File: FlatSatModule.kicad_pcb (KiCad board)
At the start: 2 copper layers, 204.5 x 269.5 mm, 2 parts, among them J101 DB26_Male_HighDensity_Mountin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

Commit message: first routing, lost schematic
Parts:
- added D1: LED, LED_SMD:LED_0805_2012Metric_Pad1.15x1.40mm_HandSolder, F.Cu at (91.4, 139.7)
- added D2: LED, LED_SMD:LED_0805_2012Metric_Pad1.15x1.40mm_HandSolder, F.Cu at (64.8, 53.3)
- added J1: HEADER_13x2, Connector_PinHeader_2.54mm:PinHeader_2x13_P2.54mm_Vertical, F.Cu at (76.2, 69.8)
- added J2: Micro_SD_Card_Det, Connector_Card:microSD_HC_Hirose_DM3D-SF, F.Cu at (91.4, 152.4)
- moved J101 126.6 mm to (83.8, 49.5), turned to 180 degrees
- moved stm32101 57.9 mm to (93.4, 99.9)
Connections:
- J101 pad 1: (no net) -> /SPI4_MOSI
- J101 pad 10: (no net) -> /SPI4_SS
- J101 pad 11: (no net) -> /SPI4_SCK
- J101 pad 12: (no net) -> /I2C1_SCL
- J101 pad 13: (no net) -> /I2C3_SDA
- J101 pad 14: (no net) -> Net-(J101-Pad14)
- J101 pad 15: (no net) -> Net-(J101-Pad15)
- J101 pad 16: (no net) -> Net-(J101-Pad16)
- J101 pad 17: (no net) -> Net-(J101-Pad17)
- J101 pad 18: (no net) -> GND
- J101 pad 19: (no net) -> /SPI4_MISO
- J101 pad 2: (no net) -> /CAN1_H
- J101 pad 20: (no net) -> /CAN1_L
- J101 pad 21: (no net) -> /I2C3_SCL
- J101 pad 22: (no net) -> /UART2_TX
- J101 pad 23: (no net) -> Net-(J101-Pad23)
- J101 pad 24: (no net) -> Net-(J101-Pad24)
- J101 pad 25: (no net) -> Net-(J101-Pad25)
- J101 pad 26: (no net) -> Net-(J101-Pad26)
- J101 pad 3: (no net) -> /I2C1_SDA
- J101 pad 4: (no net) -> /UART2_RX
- J101 pad 5: (no net) -> Net-(J101-Pad5)
- J101 pad 6: (no net) -> Net-(J101-Pad6)
- J101 pad 7: (no net) -> Net-(J101-Pad7)
- J101 pad 8: (no net) -> Net-(J101-Pad8)
- J101 pad 9: (no net) -> /VCC
- stm32101 pad 1: (no net) -> /VCC
- stm32101 pad 10: (no net) -> Net-(stm32101-Pad10)
- stm32101 pad 100: (no net) -> Net-(stm32101-Pad100)
- stm32101 pad 101: (no net) -> Net-(stm32101-Pad101)
- stm32101 pad 102: (no net) -> Net-(stm32101-Pad102)
- stm32101 pad 103: (no net) -> Net-(stm32101-Pad103)
- stm32101 pad 104: (no net) -> Net-(stm32101-Pad104)
- stm32101 pad 105: (no net) -> Net-(stm32101-Pad105)
- stm32101 pad 106: (no net) -> Net-(stm32101-Pad106)
- stm32101 pad 107: (no net) -> Net-(stm32101-Pad107)
- stm32101 pad 108: (no net) -> Net-(stm32101-Pad108)
- stm32101 pad 109: (no net) -> Net-(stm32101-Pad109)
- stm32101 pad 11: (no net) -> /SPI4_MOSI
- stm32101 pad 110: (no net) -> Net-(stm32101-Pad110)
- stm32101 pad 111: (no net) -> Net-(stm32101-Pad111)
- stm32101 pad 112: (no net) -> Net-(stm32101-Pad112)
- stm32101 pad 113: (no net) -> Net-(stm32101-Pad113)
- stm32101 pad 114: (no net) -> Net-(stm32101-Pad114)
- stm32101 pad 115: (no net) -> Net-(stm32101-Pad115)
- stm32101 pad 116: (no net) -> Net-(stm32101-Pad116)
- stm32101 pad 117: (no net) -> Net-(stm32101-Pad117)
- stm32101 pad 118: (no net) -> Net-(stm32101-Pad118)
- stm32101 pad 119: (no net) -> Net-(stm32101-Pad119)
- stm32101 pad 12: (no net) -> Net-(stm32101-Pad12)
- stm32101 pad 120: (no net) -> Net-(stm32101-Pad120)
- stm32101 pad 121: (no net) -> Net-(stm32101-Pad121)
- stm32101 pad 122: (no net) -> Net-(stm32101-Pad122)
- stm32101 pad 123: (no net) -> Net-(stm32101-Pad123)
- stm32101 pad 124: (no net) -> Net-(stm32101-Pad124)
- stm32101 pad 125: (no net) -> Net-(stm32101-Pad125)
- stm32101 pad 126: (no net) -> Net-(stm32101-Pad126)
- stm32101 pad 127: (no net) -> GND
- stm32101 pad 128: GND -> Net-(stm32101-Pad128)
- stm32101 pad 13: (no net) -> /SPI4_SS
- stm32101 pad 14: (no net) -> /SPI4_MISO
- stm32101 pad 15: (no net) -> /SPI4_SCK
- stm32101 pad 16: (no net) -> Net-(stm32101-Pad16)
- stm32101 pad 17: (no net) -> Net-(stm32101-Pad17)
- stm32101 pad 18: (no net) -> Net-(stm32101-Pad18)
- stm32101 pad 19: (no net) -> Net-(stm32101-Pad19)
- stm32101 pad 2: (no net) -> Net-(stm32101-Pad2)
- stm32101 pad 20: (no net) -> /I2C1_SDA
- stm32101 pad 21: (no net) -> Net-(stm32101-Pad21)
- stm32101 pad 22: (no net) -> Net-(stm32101-Pad22)
- stm32101 pad 23: (no net) -> /I2C1_SCL
- stm32101 pad 24: (no net) -> Net-(stm32101-Pad24)
- stm32101 pad 25: (no net) -> Net-(stm32101-Pad25)
- stm32101 pad 26: (no net) -> Net-(stm32101-Pad26)
- stm32101 pad 27: (no net) -> Net-(stm32101-Pad27)
- stm32101 pad 28: (no net) -> Net-(stm32101-Pad28)
- stm32101 pad 29: (no net) -> Net-(stm32101-Pad29)
- stm32101 pad 3: (no net) -> Net-(stm32101-Pad3)
- stm32101 pad 30: (no net) -> Net-(stm32101-Pad30)
- stm32101 pad 31: (no net) -> Net-(stm32101-Pad31)
- stm32101 pad 32: (no net) -> Net-(stm32101-Pad32)
- stm32101 pad 33: (no net) -> Net-(stm32101-Pad33)
- stm32101 pad 34: (no net) -> Net-(stm32101-Pad34)
- stm32101 pad 35: (no net) -> Net-(stm32101-Pad35)
- stm32101 pad 36: (no net) -> /UART2_RX
- stm32101 pad 37: (no net) -> /UART2_TX
- stm32101 pad 38: (no net) -> Net-(stm32101-Pad38)
- stm32101 pad 39: (no net) -> Net-(stm32101-Pad39)
- stm32101 pad 4: (no net) -> Net-(stm32101-Pad4)
- stm32101 pad 40: (no net) -> Net-(stm32101-Pad40)
- stm32101 pad 41: (no net) -> /CAN1_H
- stm32101 pad 42: (no net) -> Net-(stm32101-Pad42)
- stm32101 pad 43: (no net) -> Net-(stm32101-Pad43)
- stm32101 pad 44: (no net) -> Net-(stm32101-Pad44)
- stm32101 pad 45: (no net) -> Net-(stm32101-Pad45)
- stm32101 pad 46: (no net) -> Net-(stm32101-Pad46)
- stm32101 pad 47: (no net) -> Net-(stm32101-Pad47)
- stm32101 pad 48: (no net) -> Net-(stm32101-Pad48)
- stm32101 pad 49: (no net) -> /CAN1_L
- stm32101 pad 5: (no net) -> Net-(stm32101-Pad5)
- stm32101 pad 50: (no net) -> Net-(stm32101-Pad50)
- stm32101 pad 51: (no net) -> Net-(stm32101-Pad51)
- stm32101 pad 52: (no net) -> Net-(stm32101-Pad52)
- stm32101 pad 53: (no net) -> /I2C3_SCL
- stm32101 pad 54: (no net) -> /I2C3_SDA
- stm32101 pad 55: (no net) -> Net-(stm32101-Pad55)
- stm32101 pad 56: (no net) -> Net-(stm32101-Pad56)
- stm32101 pad 57: (no net) -> Net-(stm32101-Pad57)
- stm32101 pad 58: (no net) -> Net-(stm32101-Pad58)
- stm32101 pad 59: (no net) -> Net-(stm32101-Pad59)
- stm32101 pad 6: (no net) -> Net-(stm32101-Pad6)
- stm32101 pad 60: (no net) -> Net-(stm32101-Pad60)
- stm32101 pad 61: (no net) -> Net-(stm32101-Pad61)
- stm32101 pad 62: (no net) -> Net-(stm32101-Pad62)
- stm32101 pad 63: (no net) -> Net-(stm32101-Pad63)
- stm32101 pad 65: (no net) -> Net-(stm32101-Pad65)
- stm32101 pad 66: (no net) -> Net-(stm32101-Pad66)
- stm32101 pad 67: (no net) -> Net-(stm32101-Pad67)
- stm32101 pad 68: (no net) -> Net-(stm32101-Pad68)
- stm32101 pad 69: (no net) -> Net-(stm32101-Pad69)
- stm32101 pad 7: (no net) -> Net-(stm32101-Pad7)
- stm32101 pad 70: (no net) -> Net-(stm32101-Pad70)
- stm32101 pad 71: (no net) -> Net-(stm32101-Pad71)
- stm32101 pad 72: (no net) -> Net-(stm32101-Pad72)
- stm32101 pad 73: (no net) -> Net-(stm32101-Pad73)
- stm32101 pad 74: (no net) -> Net-(stm32101-Pad74)
- stm32101 pad 75: (no net) -> Net-(stm32101-Pad75)
- stm32101 pad 76: (no net) -> Net-(stm32101-Pad76)
- stm32101 pad 77: (no net) -> Net-(stm32101-Pad77)
- stm32101 pad 78: (no net) -> Net-(stm32101-Pad78)
- stm32101 pad 79: (no net) -> Net-(stm32101-Pad79)
- stm32101 pad 8: (no net) -> Net-(stm32101-Pad8)
- stm32101 pad 80: (no net) -> Net-(stm32101-Pad80)
- stm32101 pad 81: (no net) -> Net-(stm32101-Pad81)
- stm32101 pad 82: (no net) -> Net-(stm32101-Pad82)
- stm32101 pad 83: (no net) -> Net-(stm32101-Pad83)
- stm32101 pad 84: (no net) -> Net-(stm32101-Pad84)
- stm32101 pad 85: (no net) -> Net-(stm32101-Pad85)
- stm32101 pad 86: (no net) -> Net-(stm32101-Pad86)
- stm32101 pad 87: (no net) -> Net-(stm32101-Pad87)
- stm32101 pad 88: (no net) -> Net-(stm32101-Pad88)
- stm32101 pad 89: (no net) -> Net-(stm32101-Pad89)
- stm32101 pad 9: (no net) -> Net-(stm32101-Pad9)
- stm32101 pad 90: (no net) -> Net-(stm32101-Pad90)
- stm32101 pad 91: (no net) -> Net-(stm32101-Pad91)
- stm32101 pad 92: (no net) -> Net-(stm32101-Pad92)
- stm32101 pad 93: (no net) -> Net-(stm32101-Pad93)
- stm32101 pad 94: (no net) -> Net-(stm32101-Pad94)
- stm32101 pad 95: (no net) -> Net-(stm32101-Pad95)
- stm32101 pad 96: (no net) -> Net-(stm32101-Pad96)
- stm32101 pad 97: (no net) -> Net-(stm32101-Pad97)
- stm32101 pad 98: (no net) -> Net-(stm32101-Pad98)
- stm32101 pad 99: (no net) -> Net-(stm32101-Pad99)
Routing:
- net /CAN1_L: track 0.00 -> 136.9 mm
- net /I2C3_SCL: track 0.00 -> 123.7 mm
- net /I2C3_SDA: track 0.00 -> 109.2 mm
- net /CAN1_H: track 0.00 -> 105.6 mm, vias 0 -> 1
- net /UART2_TX: track 0.00 -> 103.8 mm
- net /SPI4_SS: track 0.00 -> 99.9 mm
- net /SPI4_MISO: track 0.00 -> 96.2 mm
- net /SPI4_SCK: track 0.00 -> 93.7 mm
- net /I2C1_SCL: track 0.00 -> 86.9 mm
- net /UART2_RX: track 0.00 -> 81.8 mm
- net /SPI4_MOSI: track 0.00 -> 76.9 mm
- net /I2C1_SDA: track 0.00 -> 68.0 mm
- net GND: track 33.5 -> 0.00 mm, vias 1 -> 0
- net /VCC: track 0.00 -> 13.9 mm
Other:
- board size 204.5 x 269.5 mm -> 69.8 x 120.7 mm
- copper layers 2 -> 4

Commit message: ?
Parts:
- added R1: R, Resistor_SMD:R_2010_5025Metric_Pad1.52x2.65mm_HandSolder, F.Cu at (71.3, 59.7)
- added R2: R, Resistor_SMD:R_2010_5025Metric_Pad1.52x2.65mm_HandSolder, F.Cu at (91.6, 133.3)
- moved D2 90.4 mm to (91.4, 139.7), turned to 0 degrees
- moved D1 84.3 mm to (64.8, 59.7)
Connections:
- D1 pad 2: Net-(D1-Pad2) -> /VCC
- D2 pad 2: Net-(D2-Pad2) -> /SD_DET
- J2 pad 10: Net-(J2-Pad10) -> /VCC
- J2 pad 9: Net-(J2-Pad9) -> /SD_DET
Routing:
- net /VCC: track 13.9 -> 122.3 mm
- net /SD_DET: track 0.00 -> 20.3 mm
- net Net-(D2-Pad1): track 0.00 -> 6.81 mm
- net Net-(D1-Pad1): track 0.00 -> 3.19 mm

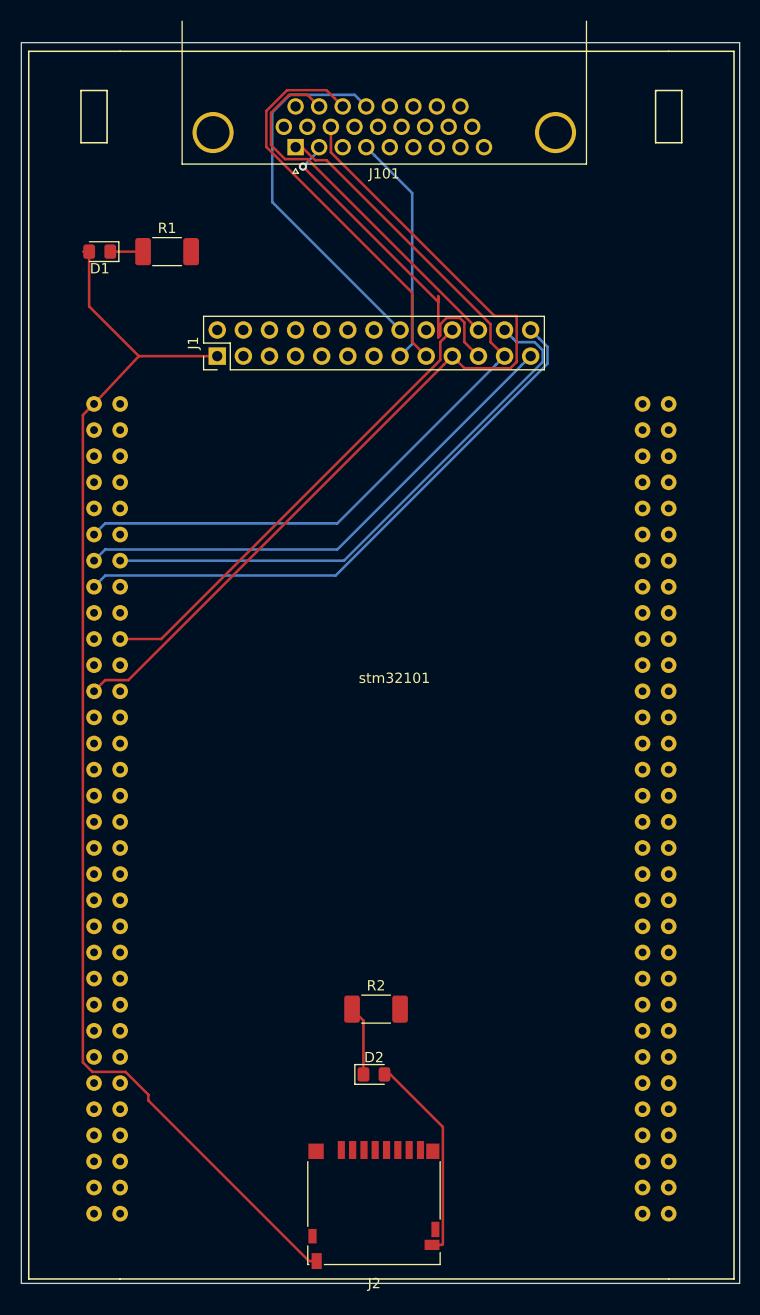
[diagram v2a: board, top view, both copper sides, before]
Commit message: updated wiring + wired SD card
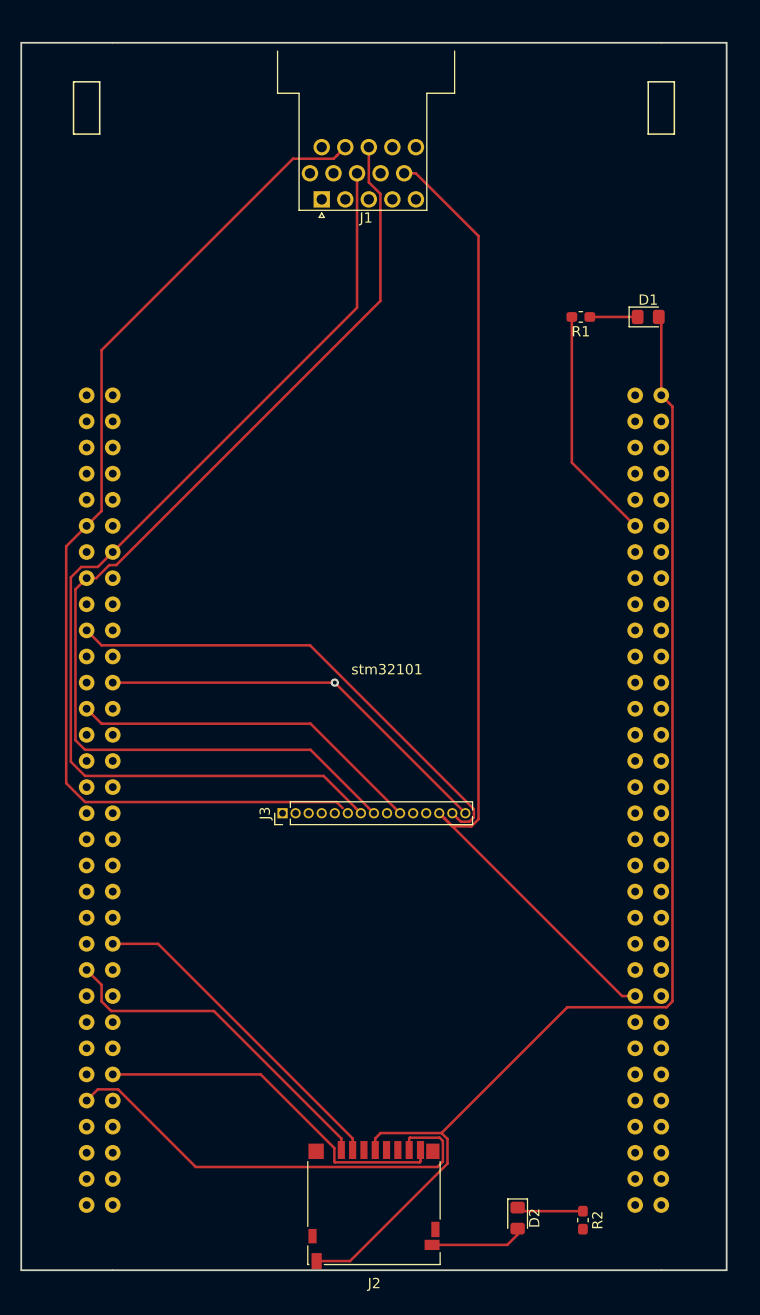
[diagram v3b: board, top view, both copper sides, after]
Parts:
- removed J101: DB26_Male_HighDensity_MountingHoles, Connector_Dsub:DSUB-26-HD_Female_Horizontal_P2.29x1.98mm_EdgePinOffset8.35mm_Housed_MountingHolesOffset10.89mm
- added J3: HEADER_15, Connector_PinHeader_1.27mm:PinHeader_1x15_P1.27mm_Vertical, F.Cu at (82.5, 114.3)
- J1: value HEADER_13x2 -> DB15_Female_HighDensity; footprint Connector_PinHeader_2.54mm:PinHeader_2x13_P2.54mm_Vertical -> Connector_Dsub:DSUB-15-HD_Female_Horizontal_P2.29x2.54mm_EdgePinOffset9.40mm
- R1, R2: footprint Resistor_SMD:R_2010_5025Metric_Pad1.52x2.65mm_HandSolder -> Resistor_SMD:R_0603_1608Metric_Pad1.05x0.95mm_HandSolder
- moved D1 53.7 mm to (118.1, 66.0), turned to 0 degrees
- moved R1 40.7 mm to (111.6, 66.0), turned to 180 degrees
- moved R2 28.7 mm to (111.8, 153.9), turned to 270 degrees
- moved D2 19.8 mm to (105.4, 153.7), turned to 270 degrees
- moved J1 18.3 mm to (86.4, 54.6), turned to 180 degrees
- moved stm32101 1.11 mm to (92.7, 99.1)
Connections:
- net Net-(J2-Pad3) renamed /SD_CMD
- net Net-(J2-Pad5) renamed /SD_CLK
- net Net-(stm32101-Pad10) renamed /PC15
- net Net-(stm32101-Pad100) renamed /PF15
- net Net-(stm32101-Pad101) renamed /PE7
- net Net-(stm32101-Pad102) renamed /PG1
- net Net-(stm32101-Pad103) renamed /PE9
- net Net-(stm32101-Pad104) renamed /PE8
- net Net-(stm32101-Pad105) renamed /PE11
- net Net-(stm32101-Pad106) renamed /PE10
- net Net-(stm32101-Pad107) renamed /PE13
- net Net-(stm32101-Pad108) renamed /PE12
- net Net-(stm32101-Pad109) renamed /PE15
- net Net-(stm32101-Pad110) renamed /PE14
- net Net-(stm32101-Pad113) renamed /PB13
- net Net-(stm32101-Pad114) renamed /PB12
- net Net-(stm32101-Pad115) renamed /PB15
- net Net-(stm32101-Pad116) renamed /PB14
- net Net-(stm32101-Pad117) renamed /PD9
- net Net-(stm32101-Pad118) renamed /PD8
- net Net-(stm32101-Pad119) renamed /PD11
- net Net-(stm32101-Pad12) renamed /PC13
- net Net-(stm32101-Pad120) renamed /PD10
- net Net-(stm32101-Pad121) renamed /PD13
- net Net-(stm32101-Pad122) renamed /PD12
- net Net-(stm32101-Pad123) renamed /PD15
- net Net-(stm32101-Pad124) renamed /PD14
- net Net-(stm32101-Pad125) renamed /PG3
- net Net-(stm32101-Pad126) renamed /PG2
- net Net-(stm32101-Pad16) renamed /PE3
- net Net-(stm32101-Pad17) renamed /PE0
- net Net-(stm32101-Pad18) renamed /PE1
- net Net-(stm32101-Pad21) renamed /BOOT0
- net Net-(stm32101-Pad22) renamed /VDD
- net Net-(stm32101-Pad26) renamed /PB5
- net Net-(stm32101-Pad27) renamed /PG15
- net Net-(stm32101-Pad28) renamed /PB3
- net Net-(stm32101-Pad29) renamed /PG13
- net Net-(stm32101-Pad3) renamed /PF4
- net Net-(stm32101-Pad30) renamed /PG14
- net Net-(stm32101-Pad31) renamed /PG11
- net Net-(stm32101-Pad32) renamed /PG12
- net Net-(stm32101-Pad33) renamed /PG9
- net Net-(stm32101-Pad34) renamed /PG10
- net Net-(stm32101-Pad35) renamed /PD7
- net Net-(stm32101-Pad38) renamed /PD4
- net Net-(stm32101-Pad39) renamed /PD3
- net Net-(stm32101-Pad4) renamed /PF5
- net Net-(stm32101-Pad40) renamed /PD2
- net Net-(stm32101-Pad42) renamed /PD0
- net Net-(stm32101-Pad43) renamed /PC12
- net Net-(stm32101-Pad46) renamed /PA15
- net Net-(stm32101-Pad47) renamed /PA14
- net Net-(stm32101-Pad48) renamed /PA13
- net Net-(stm32101-Pad5) renamed /PF2
- net Net-(stm32101-Pad50) renamed /PA11
- net Net-(stm32101-Pad51) renamed /PA10
- net Net-(stm32101-Pad52) renamed /PA9
- net Net-(stm32101-Pad56) renamed /PC7
- net Net-(stm32101-Pad57) renamed /PC6
- net Net-(stm32101-Pad58) renamed /PG8
- net Net-(stm32101-Pad59) renamed /PG7
- net Net-(stm32101-Pad6) renamed /PF3
- net Net-(stm32101-Pad60) renamed /PG6
- net Net-(stm32101-Pad61) renamed /PG5
- net Net-(stm32101-Pad62) renamed /PG4
- net Net-(stm32101-Pad67) renamed /PF6
- net Net-(stm32101-Pad68) renamed /NC
- net Net-(stm32101-Pad69) renamed /PF8
- net Net-(stm32101-Pad7) renamed /PF0
- net Net-(stm32101-Pad70) renamed /PF7
- net Net-(stm32101-Pad71) renamed /PF10
- net Net-(stm32101-Pad72) renamed /PF9
- net Net-(stm32101-Pad73) renamed /PH1
- net Net-(stm32101-Pad74) renamed /PH0
- net Net-(stm32101-Pad76) renamed /NRST
- net Net-(stm32101-Pad77) renamed /PC1
- net Net-(stm32101-Pad78) renamed /PC0
- net Net-(stm32101-Pad79) renamed /PC3
- net Net-(stm32101-Pad8) renamed /PF1
- net Net-(stm32101-Pad80) renamed /PC2
- net Net-(stm32101-Pad81) renamed /PA1
- net Net-(stm32101-Pad82) renamed /PA0
- net Net-(stm32101-Pad83) renamed /PA3
- net Net-(stm32101-Pad84) renamed /PA2
- net Net-(stm32101-Pad86) renamed /PA4
- net Net-(stm32101-Pad88) renamed /PA6
- net Net-(stm32101-Pad89) renamed /PC5
- net Net-(stm32101-Pad9) renamed /PC14
- net Net-(stm32101-Pad90) renamed /PC4
- net Net-(stm32101-Pad91) renamed /PB1
- net Net-(stm32101-Pad92) renamed /PB0
- net Net-(stm32101-Pad94) renamed /PB2
- net Net-(stm32101-Pad95) renamed /PF12
- net Net-(stm32101-Pad96) renamed /PF11
- net Net-(stm32101-Pad97) renamed /PF14
- net Net-(stm32101-Pad98) renamed /PF13
- net Net-(stm32101-Pad99) renamed /PG0
- D1 pad 2: /VCC -> VCC
- J1 pad 1: /VCC -> Net-(J1-Pad1)
- J1 pad 10: Net-(J1-Pad10) -> /I2C2_SDA
- J1 pad 12: Net-(J1-Pad12) -> /PE6
- J1 pad 13: Net-(J1-Pad13) -> /PE2
- J1 pad 14: Net-(J1-Pad14) -> /I2C2_SCL
- J1 pad 15: /UART2_RX -> /I2C1_SCL
- J1 pad 2: GND -> Net-(J1-Pad2)
- J1 pad 3: Net-(J1-Pad3) -> /PA7
- J1 pad 4: Net-(J1-Pad4) -> /PA5
- J1 pad 5: Net-(J1-Pad5) -> /I2C1_SDA
- J1 pad 8: Net-(J1-Pad8) -> /PE5
- J1 pad 9: Net-(J1-Pad9) -> /PB4
- J2 pad 1: Net-(J2-Pad1) -> /PC10
- J2 pad 10: /VCC -> VCC
- J2 pad 2: Net-(J2-Pad2) -> /PC11
- J2 pad 4: Net-(J2-Pad4) -> VCC
- J2 pad 6: Net-(J2-Pad6) -> GND
- J2 pad 7: Net-(J2-Pad7) -> /PC8
- J2 pad 8: Net-(J2-Pad8) -> /PC9
- stm32101 pad 1: /VCC -> /VCC5
- stm32101 pad 11: /SPI4_MOSI -> /PE6
- stm32101 pad 111: Net-(stm32101-Pad111) -> /I2C2_SDA
- stm32101 pad 112: Net-(stm32101-Pad112) -> /I2C2_SCL
- stm32101 pad 128: Net-(stm32101-Pad128) -> GND
- stm32101 pad 13: /SPI4_SS -> /PE4
- stm32101 pad 14: /SPI4_MISO -> /PE5
- stm32101 pad 15: /SPI4_SCK -> /PE2
- stm32101 pad 19: Net-(stm32101-Pad19) -> /I2C1_SCL
- stm32101 pad 2: Net-(stm32101-Pad2) -> /VCC5
- stm32101 pad 20: /I2C1_SDA -> /PB9
- stm32101 pad 23: /I2C1_SCL -> /PB6
- stm32101 pad 24: Net-(stm32101-Pad24) -> /I2C1_SDA
- stm32101 pad 25: Net-(stm32101-Pad25) -> /PB4
- stm32101 pad 36: /UART2_RX -> /PD6
- stm32101 pad 37: /UART2_TX -> /PD5
- stm32101 pad 41: /CAN1_H -> /PD1
- stm32101 pad 44: Net-(stm32101-Pad44) -> /PC11
- stm32101 pad 45: Net-(stm32101-Pad45) -> /PC10
- stm32101 pad 49: /CAN1_L -> /PA12
- stm32101 pad 53: /I2C3_SCL -> /PA8
- stm32101 pad 54: /I2C3_SDA -> /PC9
- stm32101 pad 55: Net-(stm32101-Pad55) -> /PC8
- stm32101 pad 63: Net-(stm32101-Pad63) -> GND
- stm32101 pad 65: Net-(stm32101-Pad65) -> VCC
- stm32101 pad 66: Net-(stm32101-Pad66) -> VCC
- stm32101 pad 75: Net-(stm32101-Pad75) -> GND
- stm32101 pad 85: Net-(stm32101-Pad85) -> /PA5
- stm32101 pad 87: Net-(stm32101-Pad87) -> /PA7
- stm32101 pad 93: Net-(stm32101-Pad93) -> GND
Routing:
- net /CAN1_L: track 136.9 -> 0.00 mm
- net /I2C3_SCL: track 123.7 -> 0.00 mm
- net VCC: track 0.00 -> 122.5 mm
- net /VCC: track 122.3 -> 0.00 mm
- net /I2C3_SDA: track 109.2 -> 0.00 mm
- net /CAN1_H: track 105.6 -> 0.00 mm, vias 1 -> 0
- net /UART2_TX: track 103.8 -> 0.00 mm
- net /PE2: track 0.00 -> 103.3 mm
- net /PE6: track 0.00 -> 103.3 mm
- net /PE5: track 0.00 -> 100.0 mm
- net /SPI4_SS: track 99.9 -> 0.00 mm
- net /PB4: track 0.00 -> 99.5 mm
- net /I2C2_SDA: track 0.00 -> 97.5 mm
- net /I2C2_SCL: track 0.00 -> 96.4 mm
- net /SPI4_MISO: track 96.2 -> 0.00 mm
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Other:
- board size 69.8 x 120.7 mm -> 68.6 x 119.4 mm
